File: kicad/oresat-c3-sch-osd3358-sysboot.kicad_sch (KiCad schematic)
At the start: 21 parts, among them J6 Conn_01x02, U1 OSD3358-512M-BSM

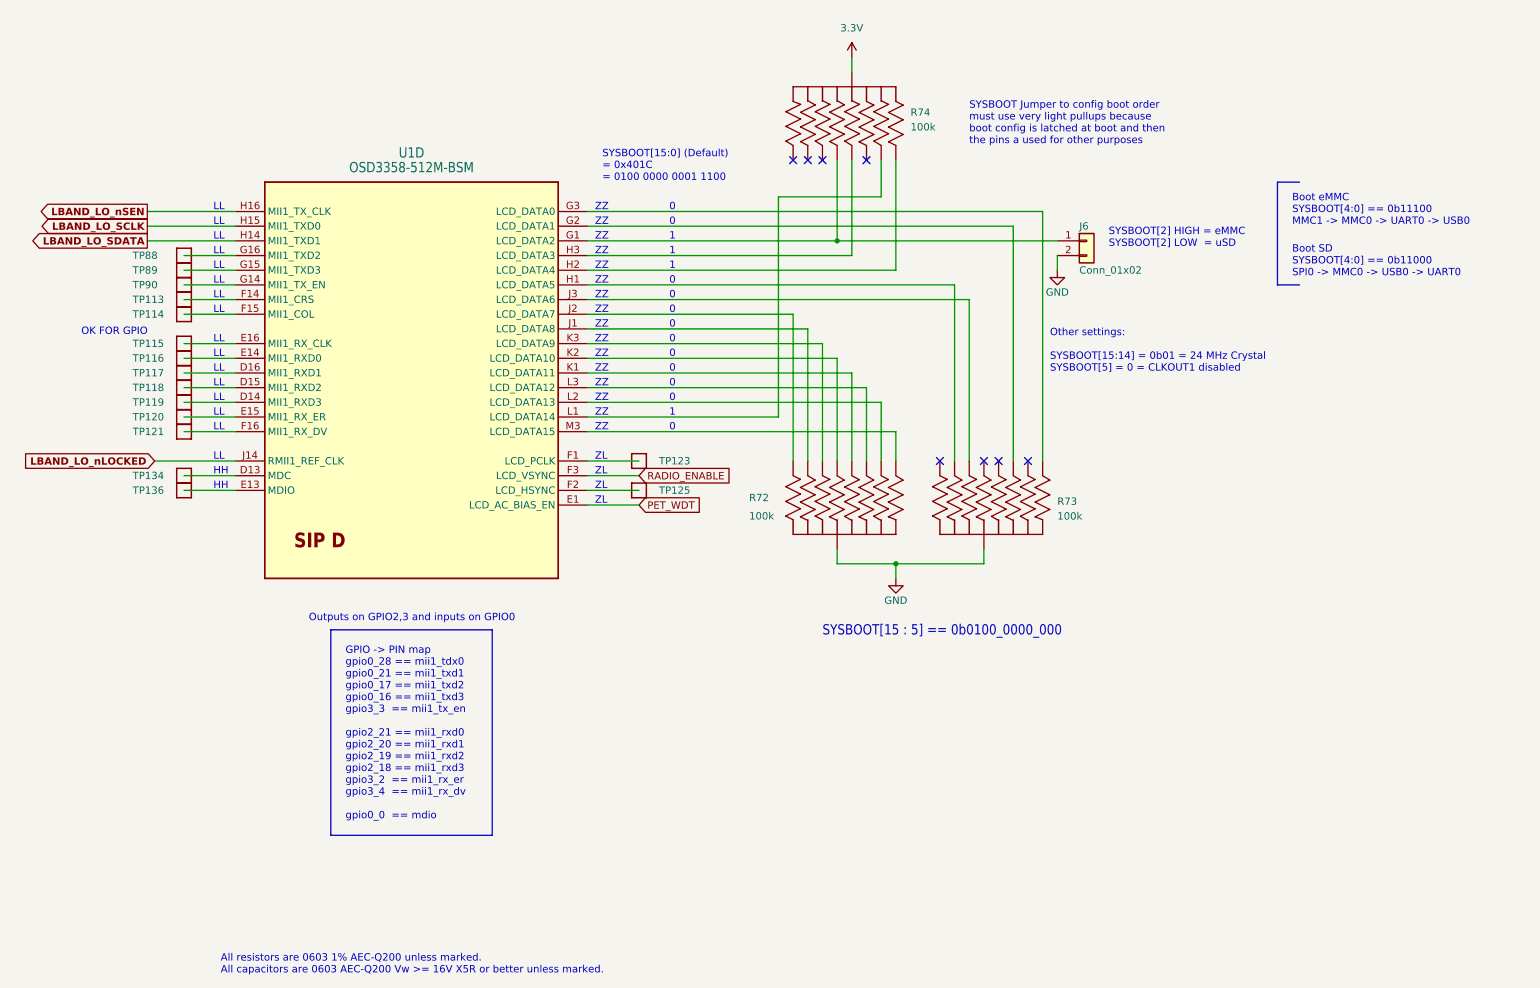
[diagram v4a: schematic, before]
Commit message: An evening of cleanups from the design review. Includes lots of ERC and DRC cleanup, although still over 450 DRC errors mostly from RF keepouts. Fixed PA ground connection, notes on pin reset configuration, and lots of small naggy things. Also cleaned up wierd broken traces on eMMC traces. No longer all same length (sorry Oliver) but it shouldn't affect performance.
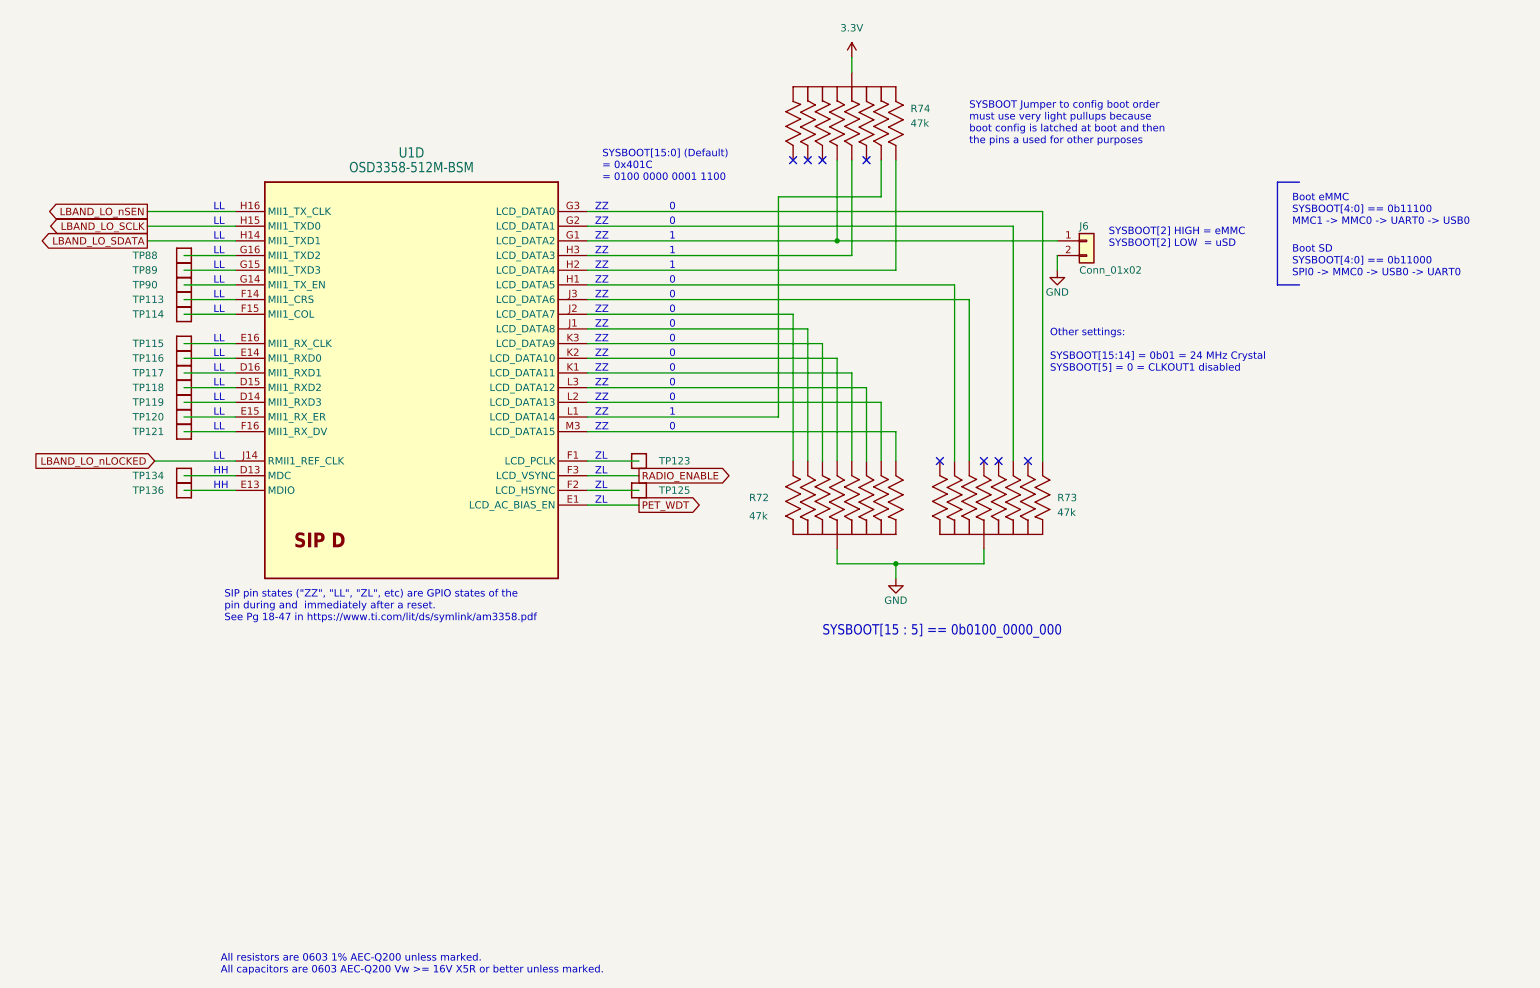
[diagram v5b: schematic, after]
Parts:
- R72, R73, R74: value 100k -> 47k
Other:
- note added: "SIP pin states ("ZZ", "LL", "ZL", etc) are GPIO states of the pin during and immediately after a reset. See Pg 18-47 in https://www.ti.com/lit/ds/symlink/am3358.pdf"
- note removed: "GPIO -> PIN map gpio0_28 == mii1_tdx0 gpio0_21 == mii1_txd1 gpio0_17 == mii1_txd2 gpio0_16 == mii1_txd3 gpio3_3 == mii1_tx_en gpio2_21 == mii1_rxd0 gpio2_20 == mii1_rxd1 gpio2_19 == mii1_rxd2 gpio2_18 == mii1_rxd3 gpio3_2 == mii1_rx_er gpio3_4 == mii1_rx_dv gpio0_0 == mdio"
- note removed: "OK FOR GPIO"
- note removed: "Outputs on GPIO2,3 and inputs on GPIO0"
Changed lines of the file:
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@@
-    (stroke (width 0) (type default))
-  )
-  (polyline (pts (xy 133.35 201.93) (xy 161.29 201.93))
     (stroke (width 0) (type default))
   )
@@
     (stroke (width 0) (type default))
   )
-  (polyline (pts (xy 133.35 201.93) (xy 133.35 237.49))
-    (stroke (width 0) (type default))
-  )
   (polyline (pts (xy 300.99 124.46) (xy 297.18 124.46))
     (stroke (width 0) (type default))
@@
     (stroke (width 0) (type default))
   )
-  (polyline (pts (xy 133.35 237.49) (xy 161.29 237.49))
-    (stroke (width 0) (type default))
-  )
   (wire (pts (xy 246.38 190.5) (xy 246.38 187.96))
     (stroke (width 0) (type default))
@@
     (stroke (width 0) (type default))
   )
-  (polyline (pts (xy 161.29 237.49) (xy 161.29 201.93))
-    (stroke (width 0) (type default))
-  )
   (wire (pts (xy 177.8 152.4) (xy 218.44 152.4))
     (stroke (width 0) (type default))
@@
   )
   (text "SYSBOOT[2] HIGH = eMMC\nSYSBOOT[2] LOW  = uSD" (at 267.97 135.89 0)
+    (effects (font (size 1.27 1.27)) (justify left bottom))
+  )
+  (text "SIP pin states (\"ZZ\", \"LL\", \"ZL\", etc) are GPIO states of the\npin during and  immediately after a reset.  \nSee Pg 18-47 in https://www.ti.com/lit/ds/symlink/am3358.pdf\n"
+    (at 114.935 200.66 0)
     (effects (font (size 1.27 1.27)) (justify left bottom))
   )
@@
     (effects (font (size 1.27 1.27)) (justify left bottom))
   )
-  (text "Outputs on GPIO2,3 and inputs on GPIO0" (at 129.54 200.66 0)
-    (effects (font (size 1.27 1.27)) (justify left bottom))
-  )
   (text "LL" (at 113.03 144.78 0)
     (effects (font (size 1.27 1.27)) (justify left bottom))
@@
     (effects (font (size 1.27 1.27)) (justify left bottom))
   )
-  (text "GPIO -> PIN map\ngpio0_28 == mii1_tdx0\ngpio0_21 == mii1_txd1\ngpio0_17 == mii1_txd2\ngpio0_16 == mii1_txd3\ngpio3_3  == mii1_tx_en\n\ngpio2_21 == mii1_rxd0\ngpio2_20 == mii1_rxd1\ngpio2_19 == mii1_rxd2\ngpio2_18 == mii1_rxd3\ngpio3_2  == mii1_rx_er\ngpio3_4  == mii1_rx_dv\n\ngpio0_0  == mdio"
-    (at 135.89 234.95 0)
-    (effects (font (size 1.27 1.27)) (justify left bottom))
-  )
-  (text "OK FOR GPIO" (at 90.17 151.13 0)
-    (effects (font (size 1.27 1.27)) (justify left bottom))
-  )
   (text "0" (at 193.04 152.4 0)
     (effects (font (size 1.27 1.27)) (justify right bottom))
@@
   )
   (global_label "LBAND_LO_nSEN" (shape output) (at 101.6 129.54 180) (fields_autoplaced)
-    (effects (font (size 1.27 1.27) (thickness 0.254) bold) (justify right))
-    (property "Intersheetrefs" "${INTERSHEET_REFS}" (at 83.1468 129.54 0)
+    (effects (font (size 1.27 1.27)) (justify right))
+    (property "Intersheetrefs" "${INTERSHEET_REFS}" (at 83.5752 129.54 0)
       (effects (font (size 1.27 1.27)) (justify right))
     )
   )
   (global_label "LBAND_LO_SDATA" (shape output) (at 101.6 134.62 180) (fields_autoplaced)
-    (effects (font (size 1.27 1.27) (thickness 0.254) bold) (justify right))
-    (property "Intersheetrefs" "${INTERSHEET_REFS}" (at 82.3605 134.62 0)
+    (effects (font (size 1.27 1.27)) (justify right))
+    (property "Intersheetrefs" "${INTERSHEET_REFS}" (at 82.7889 134.62 0)
       (effects (font (size 1.27 1.27)) (justify right))
     )
   )
   (global_label "LBAND_LO_nLOCKED" (shape input) (at 102.87 172.72 180) (fields_autoplaced)
-    (effects (font (size 1.27 1.27) (thickness 0.254) bold) (justify right))
-    (property "Intersheetrefs" "${INTERSHEET_REFS}" (at 80.7882 172.72 0)
+    (effects (font (size 1.27 1.27)) (justify right))
+    (property "Intersheetrefs" "${INTERSHEET_REFS}" (at 81.2166 172.72 0)
       (effects (font (size 1.27 1.27)) (justify right))
     )
   )
   (global_label "LBAND_LO_SCLK" (shape output) (at 101.6 132.08 180) (fields_autoplaced)
-    (effects (font (size 1.27 1.27) (thickness 0.254) bold) (justify right))
-    (property "Intersheetrefs" "${INTERSHEET_REFS}" (at 83.2072 132.08 0)
+    (effects (font (size 1.27 1.27)) (justify right))
+    (property "Intersheetrefs" "${INTERSHEET_REFS}" (at 83.6356 132.08 0)
       (effects (font (size 1.27 1.27)) (justify right))
     )
   )
-  (global_label "PET_WDT" (shape input) (at 186.69 180.34 0) (fields_autoplaced)
+  (global_label "PET_WDT" (shape output) (at 186.69 180.34 0) (fields_autoplaced)
     (effects (font (size 1.27 1.27)) (justify left))
     (property "Intersheetrefs" "${INTERSHEET_REFS}" (at 197.639 180.34 0)
@@
     )
   )
-  (global_label "RADIO_ENABLE" (shape input) (at 186.69 175.26 0) (fields_autoplaced)
+  (global_label "RADIO_ENABLE" (shape output) (at 186.69 175.26 0) (fields_autoplaced)
     (effects (font (size 1.27 1.27)) (justify left))
     (property "Intersheetrefs" "${INTERSHEET_REFS}" (at 203.1425 175.26 0)
@@
   (symbol (lib_id "oresat-passives:EXB-A10P391J") (at 256.54 185.42 270) (unit 1)
     (in_bom yes) (on_board yes) (dnp no) (fields_autoplaced)
-    (property "Reference" "R73" (at 259.08 179.7177 90)
-      (effects (font (size 1.27 1.27)) (justify left))
-    )
-    (property "Value" "100k" (at 259.08 182.2577 90)
+    (property "Reference" "R73" (at 259.08 179.0827 90)
+      (effects (font (size 1.27 1.27)) (justify left))
+    )
+    (property "Value" "47k" (at 259.08 181.6227 90)
       (effects (font (size 1.27 1.27)) (justify left))
     )
@@
       (effects (font (size 1.27 1.27)) (justify left))
     )
-    (property "Value" "100k" (at 205.74 182.2449 90)
+    (property "Value" "47k" (at 205.74 182.2449 90)
       (effects (font (size 1.27 1.27)) (justify left))
     )
@@
   (symbol (lib_id "oresat-passives:EXB-A10P391J") (at 213.36 107.95 90) (unit 1)
     (in_bom yes) (on_board yes) (dnp no) (fields_autoplaced)
-    (property "Reference" "R74" (at 233.68 112.3823 90)
+    (property "Reference" "R74" (at 233.68 111.7473 90)
       (effects (font (size 1.27 1.27)) (justify right))
     )
-    (property "Value" "100k" (at 233.68 114.9223 90)
+    (property "Value" "47k" (at 233.68 114.2873 90)
       (effects (font (size 1.27 1.27)) (justify right))
     )

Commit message: Last of the ERC and DRC errors! only polishing left.
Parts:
- R72, R73, R74: footprint oresat-footprints:R-ARRAY_EXBA-M -> oresat-passives:Panasonic_Resistor_Array_EXBA10
- U1: footprint oresat-footprints:U-Octavo-OSD335X-BGA-256 -> oresat-ics:U-Octavo-OSD335X-BGA-256
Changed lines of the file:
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@@
       (effects (font (size 1.27 1.27)) (justify left))
     )
-    (property "Footprint" "oresat-footprints:R-ARRAY_EXBA-M" (at 261.62 185.42 0)
+    (property "Footprint" "oresat-passives:Panasonic_Resistor_Array_EXBA10" (at 261.62 185.42 0)
       (effects (font (size 1.27 1.27)) hide)
     )
@@
       (effects (font (size 1.778 1.5113)))
     )
-    (property "Footprint" "oresat-footprints:U-Octavo-OSD335X-BGA-256" (at 147.32 49.53 0)
+    (property "Footprint" "oresat-ics:U-Octavo-OSD335X-BGA-256" (at 147.32 49.53 0)
       (effects (font (size 1.27 1.27)) hide)
     )
@@
       (effects (font (size 1.27 1.27)) (justify left))
     )
-    (property "Footprint" "oresat-footprints:R-ARRAY_EXBA-M" (at 236.22 185.42 0)
+    (property "Footprint" "oresat-passives:Panasonic_Resistor_Array_EXBA10" (at 236.22 185.42 0)
       (effects (font (size 1.27 1.27)) hide)
     )
@@
       (effects (font (size 1.27 1.27)) (justify right))
     )
-    (property "Footprint" "oresat-footprints:R-ARRAY_EXBA-M" (at 208.28 107.95 0)
-      (effects (font (size 1.27 1.27)) hide)
-    )
+    (property "Footprint" "oresat-passives:Panasonic_Resistor_Array_EXBA10" (at 208.28 107.95 0)
+      (effects (font (size 1.27 1.27)) hide)
+    )

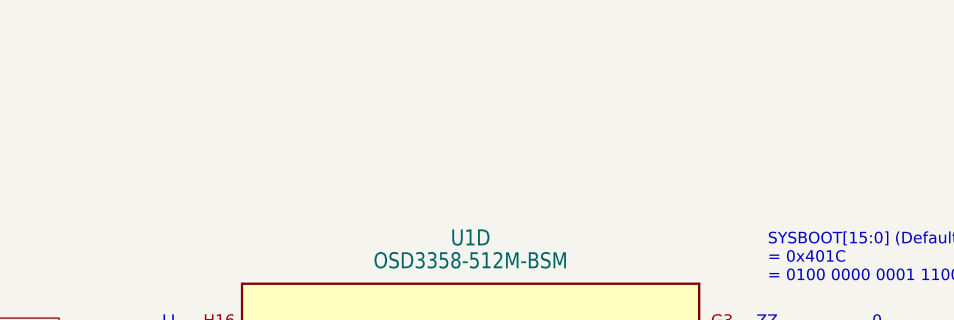
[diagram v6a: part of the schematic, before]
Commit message: More polish; fixed all non-RF DRCs.
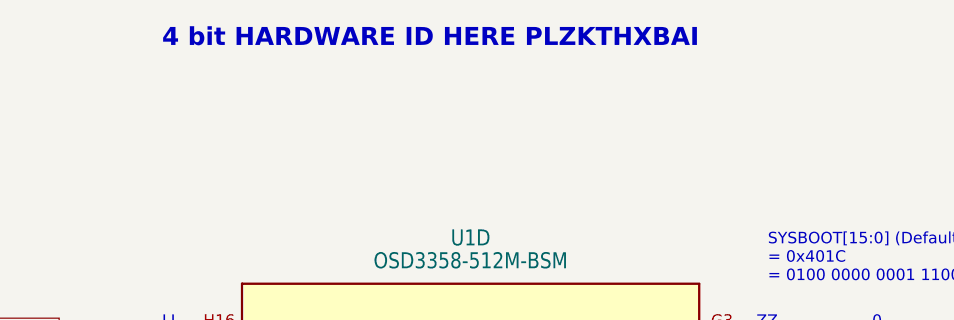
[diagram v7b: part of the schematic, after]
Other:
- note added: "4 bit HARDWARE ID HERE PLZKTHXBAI"
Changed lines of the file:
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@@
     (effects (font (size 1.27 1.27)) (justify right bottom))
+  )
+  (text "4 bit HARDWARE ID HERE PLZKTHXBAI" (at 113.03 98.425 0)
+    (effects (font (size 2 2) (thickness 0.4) bold (color 255 0 0 1)) (justify left bottom))
   )
   (text "1" (at 193.04 134.62 0)

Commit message: More fixes. TOT_CLEAR moved to a non HH pin, cleaned up in2 zones, moved fiducials, set dv/dt on power switches, added HW ID (5 bits) rechecked ADC 1.8V limits and fixed resistor values to match.
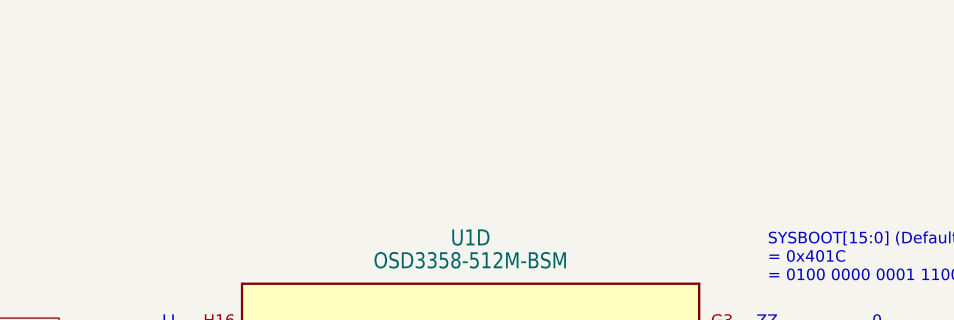
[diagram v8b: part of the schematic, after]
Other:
- note removed: "4 bit HARDWARE ID HERE PLZKTHXBAI"
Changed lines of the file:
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@@
     (effects (font (size 1.27 1.27)) (justify right bottom))
-  )
-  (text "4 bit HARDWARE ID HERE PLZKTHXBAI" (at 113.03 98.425 0)
-    (effects (font (size 2 2) (thickness 0.4) bold (color 255 0 0 1)) (justify left bottom))
   )
   (text "1" (at 193.04 134.62 0)
